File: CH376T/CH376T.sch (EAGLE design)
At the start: 14 parts

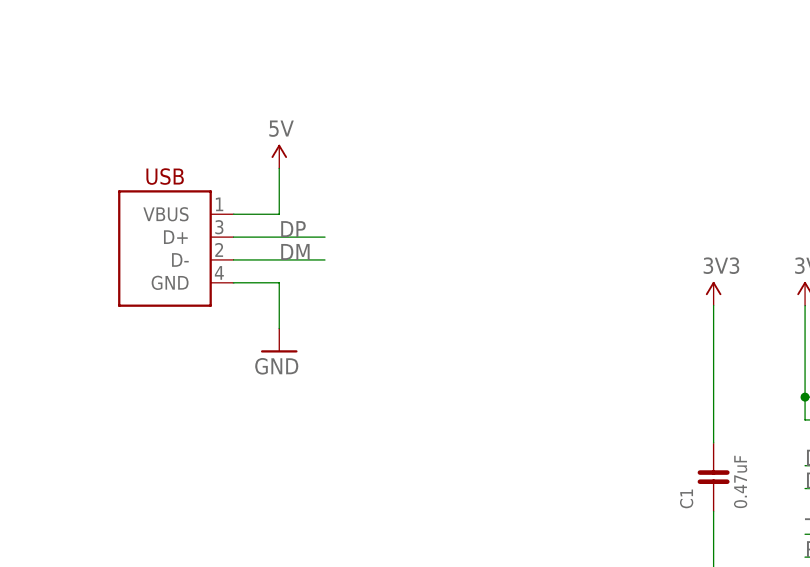
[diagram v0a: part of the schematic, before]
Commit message: add resister
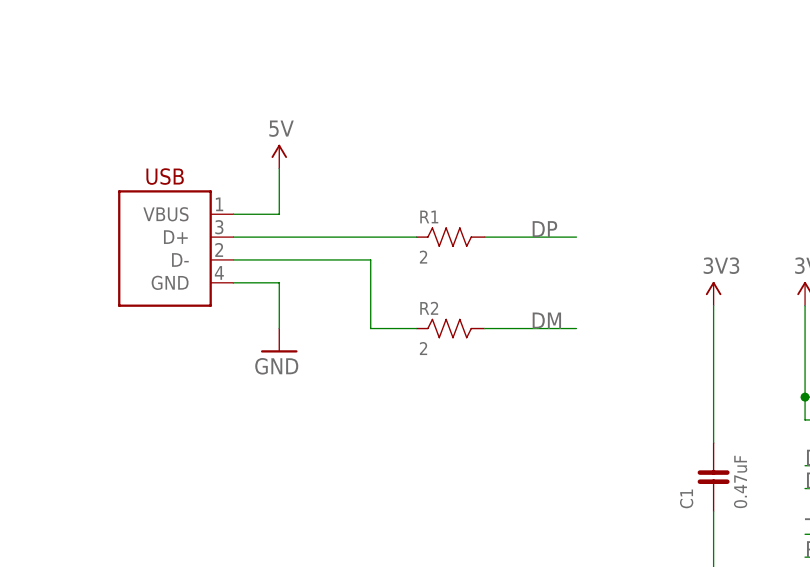
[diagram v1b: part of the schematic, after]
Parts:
- added R1, R2: 2, FaBo-Resistors:RESISTOR-0603-NARROW
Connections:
- new net N$1: R1.1, USB1.D+
- new net N$2: R2.1, USB1.D-
- net DM: now also R2.2; no longer USB1.D-
- net DP: now also R1.2; no longer USB1.D+
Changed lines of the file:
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@@
 <part name="CN2" library="FaBo-PIN" deviceset="PIN_HEADER_1X10" device=""/>
 <part name="CN3" library="FaBo-PIN" deviceset="PIN_HEADER_1X1" device=""/>
+<part name="R1" library="FaBo-Resistors" deviceset="RESISTOR" device="-0603-NARROW" value="2"/>
+<part name="R2" library="FaBo-Resistors" deviceset="RESISTOR" device="-0603-NARROW" value="2"/>
 </parts>
 <sheets>
@@
 <instance part="CN2" gate="G$1" x="220.98" y="134.62" rot="R90"/>
 <instance part="CN3" gate="G$1" x="223.52" y="154.94" rot="R90"/>
+<instance part="R1" gate="G$1" x="73.66" y="127"/>
+<instance part="R2" gate="G$1" x="73.66" y="116.84"/>
 </instances>
 <busses>
@@
 <net name="DP" class="0">
 <segment>
-<pinref part="USB1" gate="G$1" pin="D+"/>
-<wire x1="60.96" y1="127" x2="50.8" y2="127" width="0.1524" layer="91"/>
-<label x="55.88" y="127" size="1.778" layer="95"/>
-</segment>
-<segment>
 <pinref part="IC2" gate="G$1" pin="UD+"/>
 <wire x1="114.3" y1="99.06" x2="124.46" y2="99.06" width="0.1524" layer="91"/>
@@
 <label x="185.42" y="127" size="1.778" layer="95"/>
 </segment>
+<segment>
+<wire x1="88.9" y1="127" x2="78.74" y2="127" width="0.1524" layer="91"/>
+<pinref part="R1" gate="G$1" pin="2"/>
+<label x="83.82" y="127" size="1.778" layer="95"/>
+</segment>
 </net>
 <net name="DM" class="0">
-<segment>
-<pinref part="USB1" gate="G$1" pin="D-"/>
-<wire x1="60.96" y1="124.46" x2="50.8" y2="124.46" width="0.1524" layer="91"/>
-<label x="55.88" y="124.46" size="1.778" layer="95"/>
-</segment>
 <segment>
 <pinref part="IC2" gate="G$1" pin="UD-"/>
@@
 <label x="185.42" y="124.46" size="1.778" layer="95"/>
 </segment>
+<segment>
+<pinref part="R2" gate="G$1" pin="2"/>
+<wire x1="88.9" y1="116.84" x2="78.74" y2="116.84" width="0.1524" layer="91"/>
+<label x="83.82" y="116.84" size="1.778" layer="95"/>
+</segment>
 </net>
 <net name="SCS" class="0">
@@
 </segment>
 </net>
+<net name="N$1" class="0">
+<segment>
+<pinref part="USB1" gate="G$1" pin="D+"/>
+<pinref part="R1" gate="G$1" pin="1"/>
+<wire x1="50.8" y1="127" x2="71.12" y2="127" width="0.1524" layer="91"/>
+</segment>
+</net>
+<net name="N$2" class="0">
+<segment>
+<pinref part="USB1" gate="G$1" pin="D-"/>
+<wire x1="50.8" y1="124.46" x2="66.04" y2="124.46" width="0.1524" layer="91"/>
+<wire x1="66.04" y1="124.46" x2="66.04" y2="116.84" width="0.1524" layer="91"/>
+<pinref part="R2" gate="G$1" pin="1"/>
+<wire x1="66.04" y1="116.84" x2="71.12" y2="116.84" width="0.1524" layer="91"/>
+</segment>
+</net>
